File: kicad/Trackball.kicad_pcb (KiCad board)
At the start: 2 copper layers, 60 x 55 mm, 31 parts, among them J1 Conn_01x04, J101 Conn_02x03_Counter_Clockwise, SW1 Push_Button, SW102 Push_Button, SW103 Push_Button, SW106 Push_Button, SW2 Push_Button, SW3 RotaryEncoder_Switch_MP, U103 TCR2EF19, U2 PMW3360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

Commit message: up3
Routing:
- net EN: track 41.8 -> 37.3 mm, vias 2 -> 3
- net GPIO0: track 57.0 -> 54.7 mm
- net +3V3: track 100.0 -> 100.7 mm
- net Net-(SW102-B): track 11.9 -> 12.4 mm
- net +5V: track 73.6 -> 74.1 mm
- net GND: vias 22 -> 674

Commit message: update
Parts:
- added Brd101: SSD1306, SSD1306:128x64OLED, F.Cu at (159.8, 48.3)
- added D101: LED_3mm, LED_THT:LED_D3.0mm, F.Cu at (150.6, 29.9)
- added D102: LED_3mm, LED_THT:LED_D3.0mm, F.Cu at (150.5, 65.8)
- added R105: R_1206, PCM_4ms_Resistor:R_0805_2012Metric, F.Cu at (145.2, 30.9)
- added R106: R_1206, PCM_4ms_Resistor:R_0805_2012Metric, F.Cu at (145.4, 64.8)
- added SW101: Push_Button, PCM_openinput:SW_Micro_Switch, F.Cu at (137.5, 38.0)
- added SW104: Push_Button, PCM_openinput:SW_Micro_Switch, F.Cu at (137.5, 59.0)
- SW103: moved to B.Cu
- U2: moved to F.Cu
- moved SW103 40.0 mm to (98.0, 32.6), turned to -90 degrees
- moved SW106 30.4 mm to (98.0, 32.6)
- moved C110 30.0 mm to (93.7, 34.6)
- moved R102 17.6 mm to (113.0, 44.9)
- moved R101 16.6 mm to (116.9, 42.5), turned to 180 degrees
- moved C108 16.0 mm to (104.8, 69.2), turned to 90 degrees
- moved C101 14.0 mm to (122.2, 44.5)
- moved C102 14.0 mm to (122.2, 46.5)
- moved C104 12.3 mm to (117.8, 27.3)
- moved U2 11.8 mm to (118.5, 29.4)
- moved C107 2.80 mm to (117.8, 25.2), turned to 0 degrees
- moved C111 2.06 mm to (116.5, 47.9), turned to 90 degrees
- moved R104 2.06 mm to (114.0, 47.9), turned to -90 degrees
- moved U103 2.06 mm to (114.0, 24.1), turned to -90 degrees
- moved R103 1.29 mm to (100.5, 69.2), turned to 90 degrees
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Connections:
- C101 pad 1: GPIO10 -> GPIO21
- C102 pad 2: GPIO09 -> GPIO37
- SW1 pad 2: GPIO46 -> GPIO25
- SW2 pad 2: GPIO3 -> GPIO46
- SW3 pad A: GPIO10 -> GPIO21
- SW3 pad B: GPIO09 -> GPIO37
- SW3 pad S1: GPIO38 -> GPIO14
- U7 pad 17: GPIO09 -> unconnected-(U7-GPIO9/TOUCH9/ADC1_CH8/FSPIHD/SUBSPIHD-Pad17)
- U7 pad 18: GPIO10 -> unconnected-(U7-GPIO10/TOUCH10/ADC1_CH9/FSPICS0/FSPIIO4/SUBSPICS0-Pad18)
- U7 pad 19: unconnected-(U7-GPIO11/TOUCH11/ADC2_CH0/FSPID/FSPIIO5/SUBSPID-Pad19) -> GPIO11
- U7 pad 20: unconnected-(U7-GPIO12/TOUCH12/ADC2_CH1/FSPICLK/FSPIIO6/SUBSPICLK-Pad20) -> GPIO12
- U7 pad 21: unconnected-(U7-GPIO13/TOUCH13/ADC2_CH2/FSPIQ/FSPIIO7/SUBSPIQ-Pad21) -> GPIO13
- U7 pad 22: unconnected-(U7-GPIO14/TOUCH14/ADC2_CH3/FSPIWP/FSPIDQS/SUBSPIWP-Pad22) -> GPIO14
- U7 pad 23: unconnected-(U7-GPIO21-Pad23) -> GPIO21
- U7 pad 24: unconnected-(U7-GPIO47/SPICLK_P/SUBSPICLK_P_DIFF-Pad24) -> GPIO37
- U7 pad 25: unconnected-(U7-GPIO48/SPICLK_N/SUBSPICLK_N_DIFF-Pad25) -> GPIO25
- U7 pad 32: SCLK -> NCS
- U7 pad 33: MOSI -> MISO
- U7 pad 34: MISO -> MOSI
- U7 pad 35: NCS -> SCLK
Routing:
- net GPIO11: track 0.00 -> 51.9 mm
- net GPIO12: track 0.00 -> 46.3 mm
- net +3V3: track 100.7 -> 145.5 mm
- net GND: track 38.8 -> 0.00 mm, vias 674 -> 580
- net GPIO25: track 0.00 -> 35.9 mm, vias 0 -> 1
- net Net-(U2-LED_P): track 35.9 -> 2.36 mm, vias 1 -> 0
- net GPIO21: track 0.00 -> 30.7 mm
- net GPIO10: track 28.7 -> 0.00 mm
- net GPIO09: track 28.5 -> 0.00 mm, vias 1 -> 0
- net GPIO38: track 25.3 -> 50.1 mm, vias 0 -> 2
- net GPIO14: track 0.00 -> 24.3 mm, vias 0 -> 1
- net GPIO37: track 0.00 -> 20.0 mm
- net GPIO0: track 54.7 -> 74.7 mm
- net EN: track 37.3 -> 56.2 mm, vias 3 -> 1
- net +1V8: track 13.7 -> 31.6 mm, vias 1 -> 0
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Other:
- outline, holes or cut-outs redrawn
- board text removed: "RP2040 + PMW3360"

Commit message: V1 prebuild
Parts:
- added J2: Conn_02x04_Counter_Clockwise, RP2040:IDC-Header_2x04_P2.54mm_Vertical, F.Cu at (123.4, 73.1)
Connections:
- U7 pad 12: unconnected-(U7-GPIO8/TOUCH8/ADC1_CH7/SUBSPICS1-Pad12) -> GPIO8
- U7 pad 17: unconnected-(U7-GPIO9/TOUCH9/ADC1_CH8/FSPIHD/SUBSPIHD-Pad17) -> GPIO9
- U7 pad 18: unconnected-(U7-GPIO10/TOUCH10/ADC1_CH9/FSPICS0/FSPIIO4/SUBSPICS0-Pad18) -> GPIO10
- U7 pad 26: unconnected-(U7-GPIO45-Pad26) -> GPIO45
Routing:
- net +3V3: track 145.5 -> 192.9 mm, vias 2 -> 4
- net GPIO45: track 0.00 -> 29.6 mm, vias 0 -> 2
- net GPIO13: track 0.00 -> 27.4 mm, vias 0 -> 2
- net GPIO10: track 0.00 -> 19.8 mm, vias 0 -> 2
- net GPIO46: track 28.8 -> 46.6 mm
- net GPIO18: track 0.00 -> 17.5 mm, vias 0 -> 2
- net GPIO8: track 0.00 -> 17.3 mm, vias 0 -> 2
- net GPIO9: track 0.00 -> 11.1 mm, vias 0 -> 2
- net GPIO14: track 24.3 -> 34.7 mm, vias 1 -> 0
- net RX: track 26.5 -> 33.1 mm
- net TX: track 27.6 -> 33.0 mm
- net EN: track 56.2 -> 60.7 mm
- net NCS: track 18.0 -> 14.0 mm, vias 1 -> 0
- net +5V: track 70.1 -> 73.2 mm, vias 2 -> 1
- net Net-(SW102-B): track 10.9 -> 13.4 mm
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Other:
- outline, holes or cut-outs redrawn
- board text added: "+1.8V"
- board text added: "+1.8V>"
- board text added: "+3.3V"
- board text added: "+3.3V>"
- board text added: "+5V"
- board text added: "+5V>"
- board text added: "0.1uF>"
- board text added: "10K>"
- board text added: "1uF"
- board text added: "<0.1uF"
- board text added: "<10K"
- board text added: "<1uF"
- board text added: "<39"
- board text added: "<4.7uF"
- board text added: "<EN"
- board text added: "<GPIO0"
- board text added: "<GPIO10"
- board text added: "<GPIO13"
- board text added: "<GPIO25"
- board text added: "<GPIO45"
- board text added: "<GPIO46"
- board text added: "COM>"
- board text added: "D+"
- board text added: "D-"
- board text added: "DIR-GPIO21>"
- board text added: "DIR-GPIO37>"
- board text added: "GND"
- board text added: "GND>"
- board text added: "GPIO02-Motion>"
- board text added: "GPIO03"
- board text added: "GPIO08>"
- board text added: "GPIO09>"
- board text added: "GPIO11-SCL>"
- board text added: "GPIO11-SDA>"
- board text added: "GPIO18>"
- board text added: "GPIO38"
- board text added: "GPIO39-NCS>"
- board text added: "GPIO40-MISO>"
- board text added: "GPIO41-MOSI>"
- board text added: "GPIO42-SCLK>"
- board text added: "LED>"
- board text added: "LEFT Click"
- board text added: "MaSe"
- board text added: "Push_GPIO21>"
- board text added: "RIGHT Click"

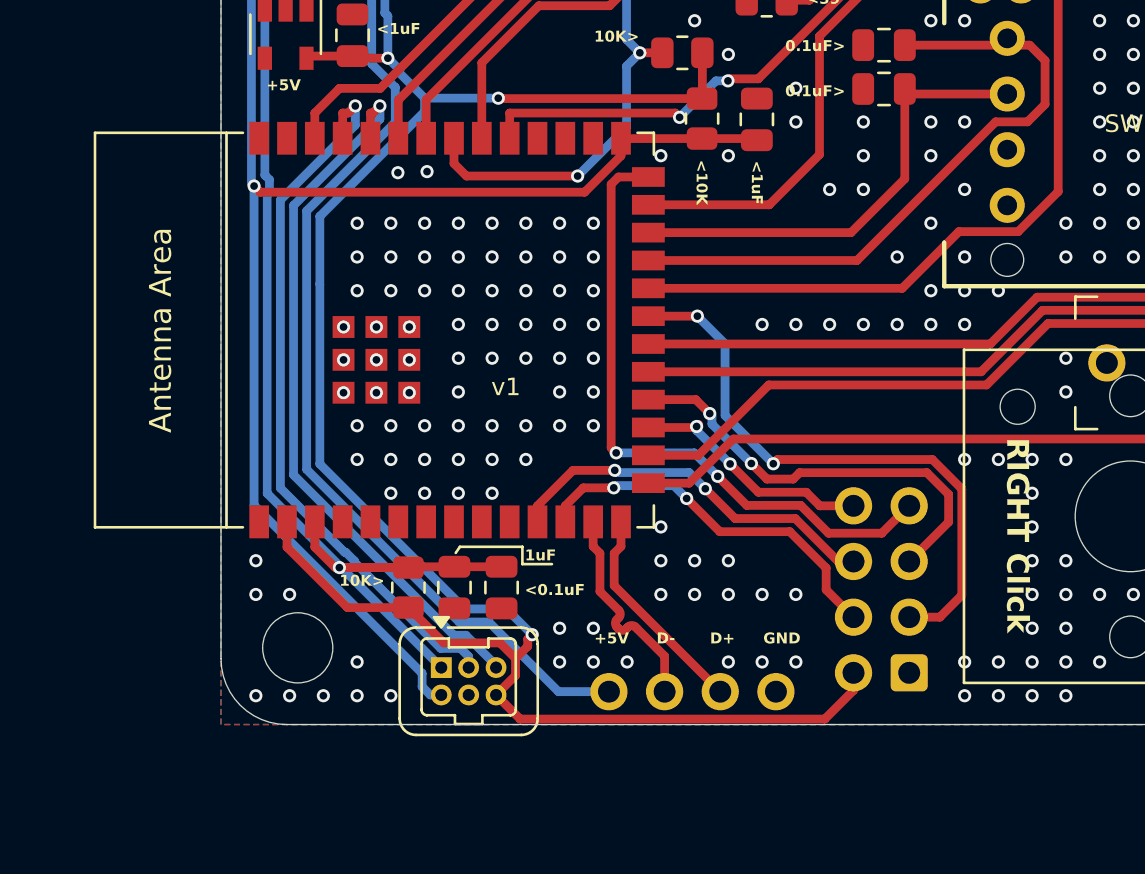
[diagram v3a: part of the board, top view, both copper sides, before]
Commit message: changement wroom 2 a 1
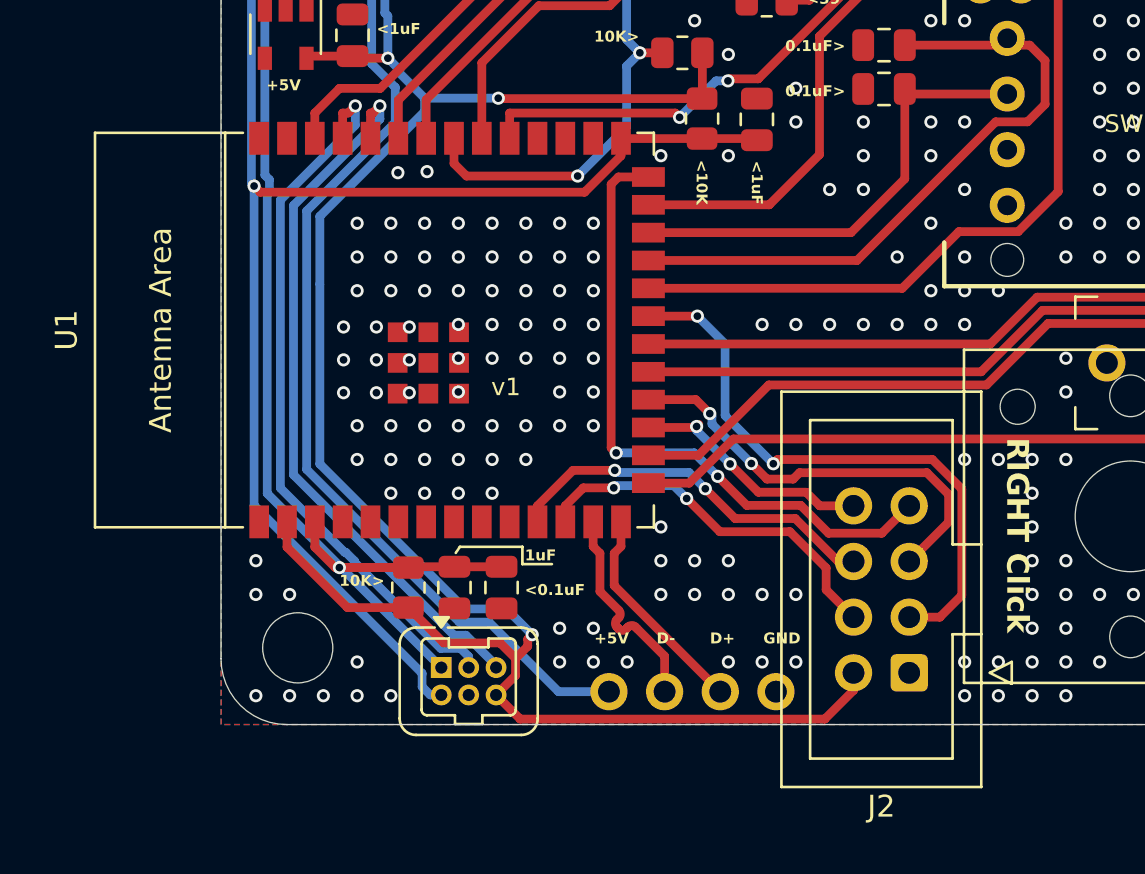
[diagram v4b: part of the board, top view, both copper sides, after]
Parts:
- removed U7: ESP32-S3-WROOM-2, PCM_Espressif:ESP32-S3-WROOM-2
- added U1: ESP32-S3-WROOM-1, PCM_Espressif:ESP32-S3-WROOM-1, F.Cu at (102.0, 57.5)
- J2: footprint RP2040:IDC-Header_2x04_P2.54mm_Vertical -> Connector_IDC:IDC-Header_2x04_P2.54mm_Vertical

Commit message: ajoute pin reset capteur optique
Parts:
- added R107: ?, Resistor_SMD:R_0805_2012Metric, F.Cu at (102.6, 30.8)
- added R108: ?, Resistor_SMD:R_0805_2012Metric, F.Cu at (101.4, 40.5)
- added R109: ?, Resistor_SMD:R_0805_2012Metric, F.Cu at (101.4, 42.6)
- moved C105 0.85 mm to (98.0, 43.2)
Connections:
- U1 pad 39: unconnected-(U1-GPIO1/TOUCH1/ADC1_CH0-Pad39) -> GPIO1
- U2 pad 7: unconnected-(U2-NRESET-Pad7) -> Net-(U2-NRESET)
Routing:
- net GPIO1: track 0.00 -> 21.9 mm
- net Net-(U2-NRESET): track 0.00 -> 8.28 mm
- net +3V3: track 192.9 -> 197.0 mm
- net MOTION: track 13.4 -> 15.3 mm
- net SCLK: track 11.4 -> 13.0 mm
- net MOSI: track 12.0 -> 12.9 mm
- net NCS: track 14.0 -> 13.2 mm
- net GND: vias 474 -> 9
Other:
- board text added: "<TCR2EF19"
- board text added: "<rst+"
- board text added: "<rst-"
- board text added: "<rst-GPIO1"
- board text added: "TLV73333PDBV"
